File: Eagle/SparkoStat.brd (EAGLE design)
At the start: 79.8 x 49 mm, 30 parts, among them IC1 MIC4680-5.0YM, K1 AQY282EHA, K2 AQY282EHA, K3 AQY282EHA, K4 AQY282EHA, Q1 NPN

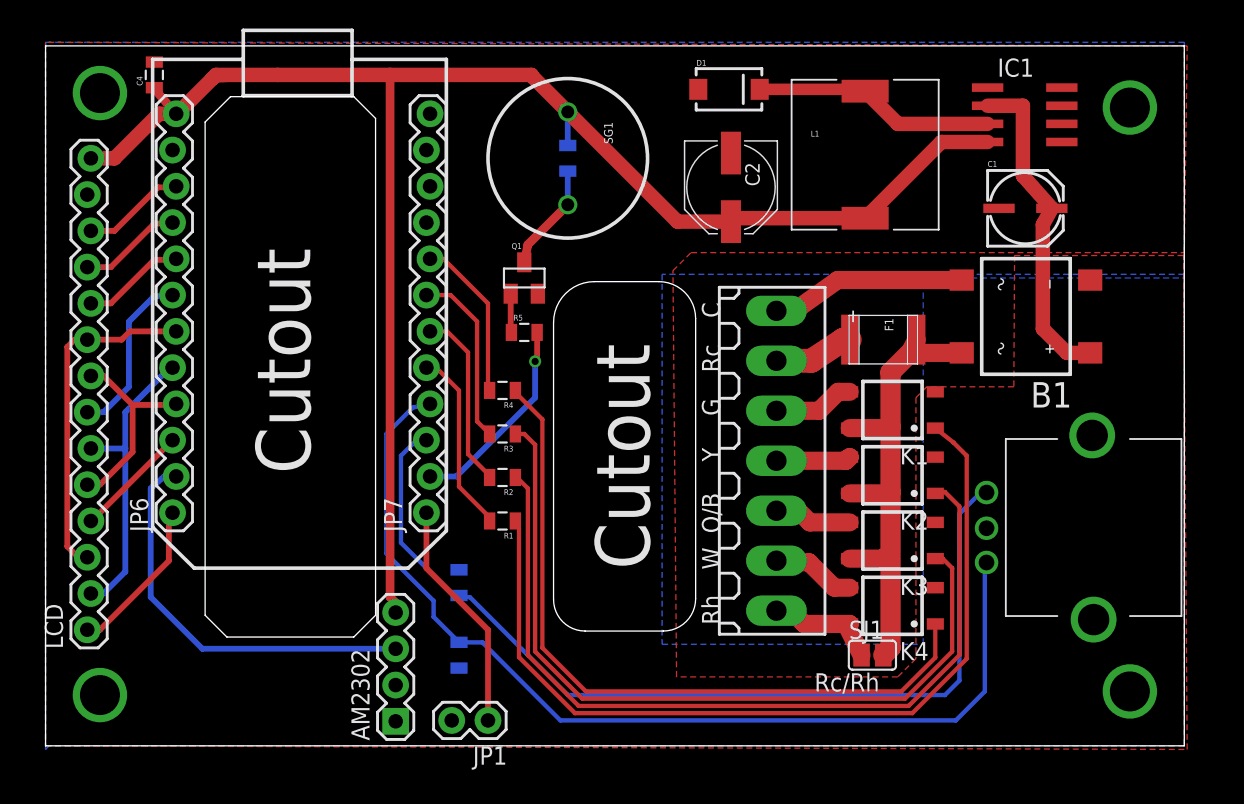
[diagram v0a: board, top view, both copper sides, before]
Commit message: Changed DHT22 to verticle
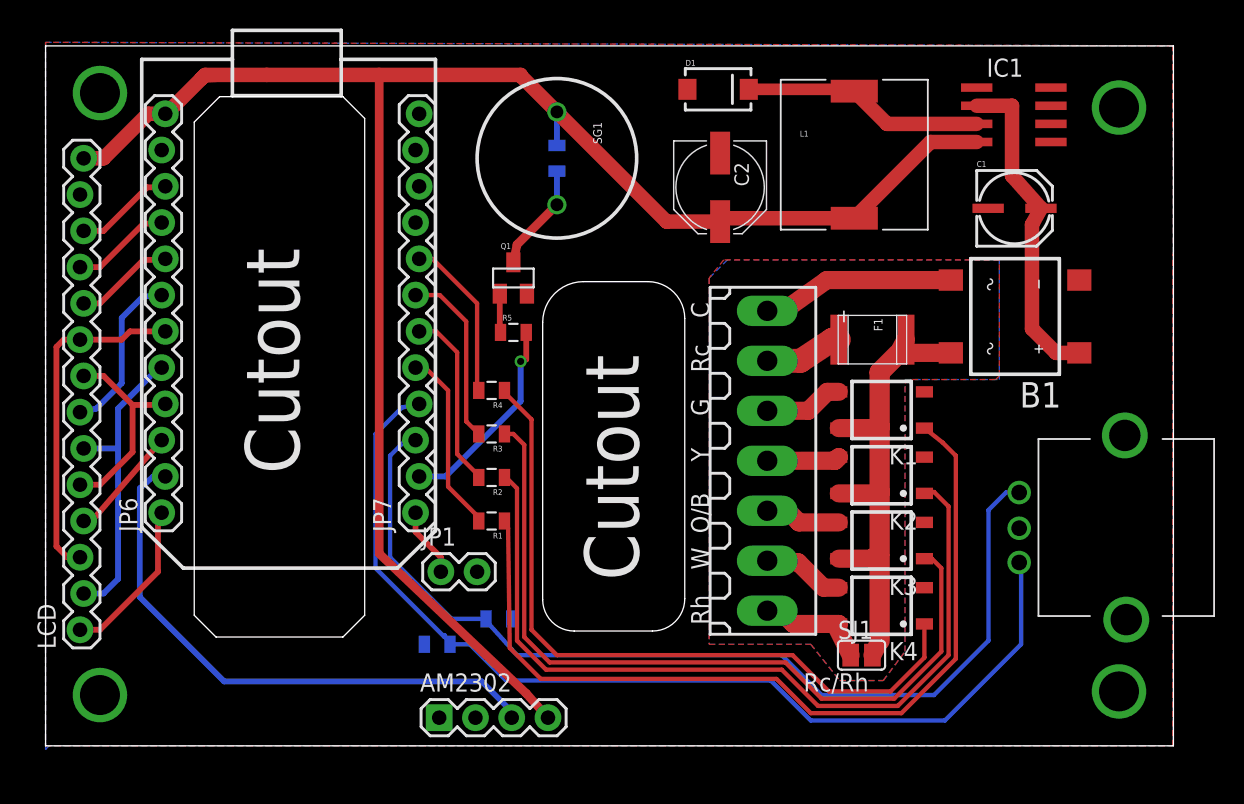
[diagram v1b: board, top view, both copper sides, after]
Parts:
- removed C4: 0.1uF, SparkFun-Capacitors:0805
- moved JP1 10.9 mm to (27.7, 12.2), turned to 0 degrees
- moved C6 3.78 mm to (31.8, 8.89), turned to 180 degrees
- moved AM2302 3.06 mm to (27.6, 1.97), turned to 0 degrees
- moved ENC 2.29 mm to (75.7, 15.2)
- moved C5 1.70 mm to (27.4, 7.11), turned to 0 degrees
- moved B1 0.76 mm to (67.9, 30.1)
- moved C1 0.76 mm to (67.8, 37.8)
- moved C2 0.76 mm to (47.2, 39.1)
- moved C3 0.76 mm to (35.8, 41.1)
- moved D1 0.76 mm to (47.1, 46.0)
- moved F1 0.76 mm to (57.9, 28.4)
- moved IC1 0.76 mm to (67.8, 44.2)
- moved JP6 0.76 mm to (8.26, 16.3)
- moved JP7 0.76 mm to (26.0, 16.3)
- moved K1 0.76 mm to (58.6, 23.5)
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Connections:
- net +5V: no longer C4.1
- net GND: no longer C4.2
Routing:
- net OPT: track 16.3 -> 4.87 mm
- net DHT: track 28.4 -> 39.6 mm
- net +5V: track 119.8 -> 129.3 mm
- net ENC_A: track 66.5 -> 68.8 mm
- net ENC_B: track 69.6 -> 71.4 mm
- net N$11: track 51.1 -> 50.4 mm
- net N$10: track 55.4 -> 54.8 mm
- net N$7: track 58.6 -> 58.0 mm
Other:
- board size 79.8 x 49 mm -> 79 x 49 mm
